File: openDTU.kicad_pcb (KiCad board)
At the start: 2 copper layers, 50 x 50 mm, 3 parts, among them U1 ESP32NodeMCU, U2 NRF24L01+PA+LNA_Breakout

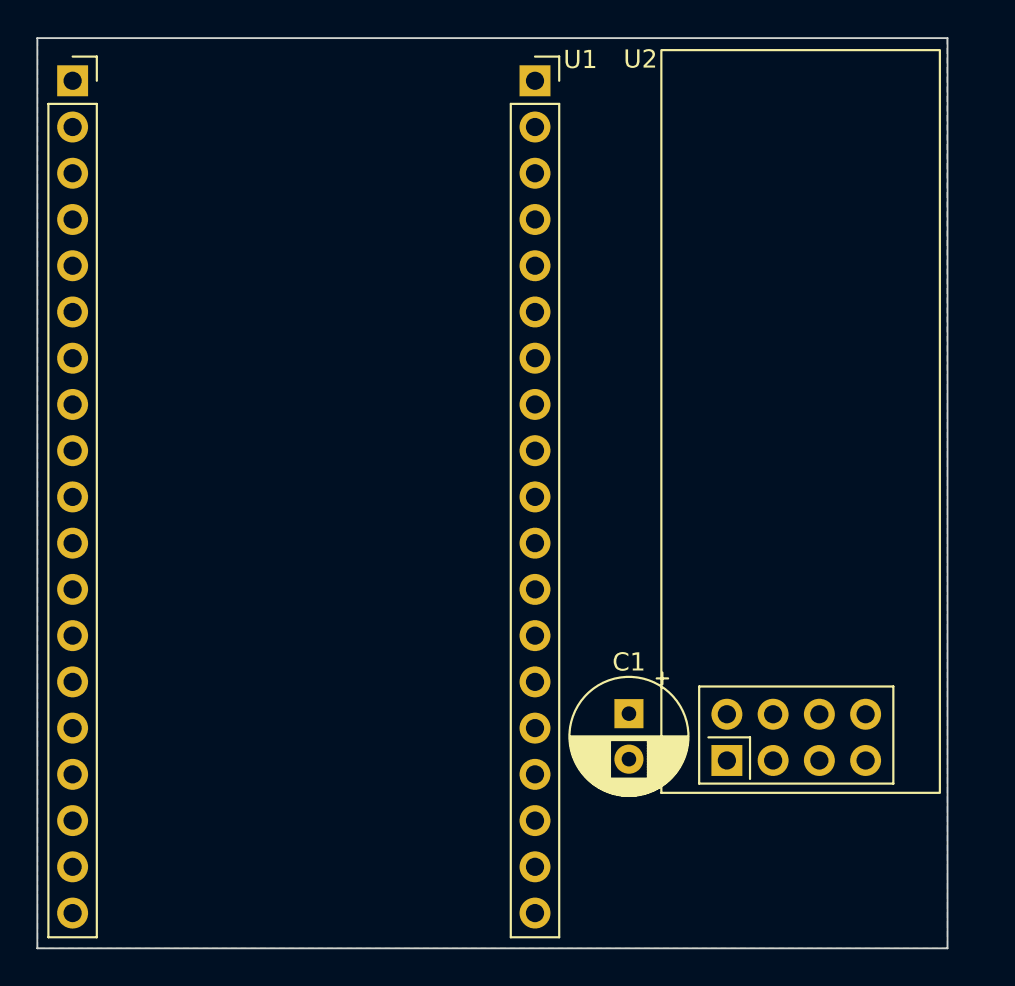
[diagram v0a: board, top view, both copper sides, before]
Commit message: connecting nRF24L01+ to the ESP32 in schematic
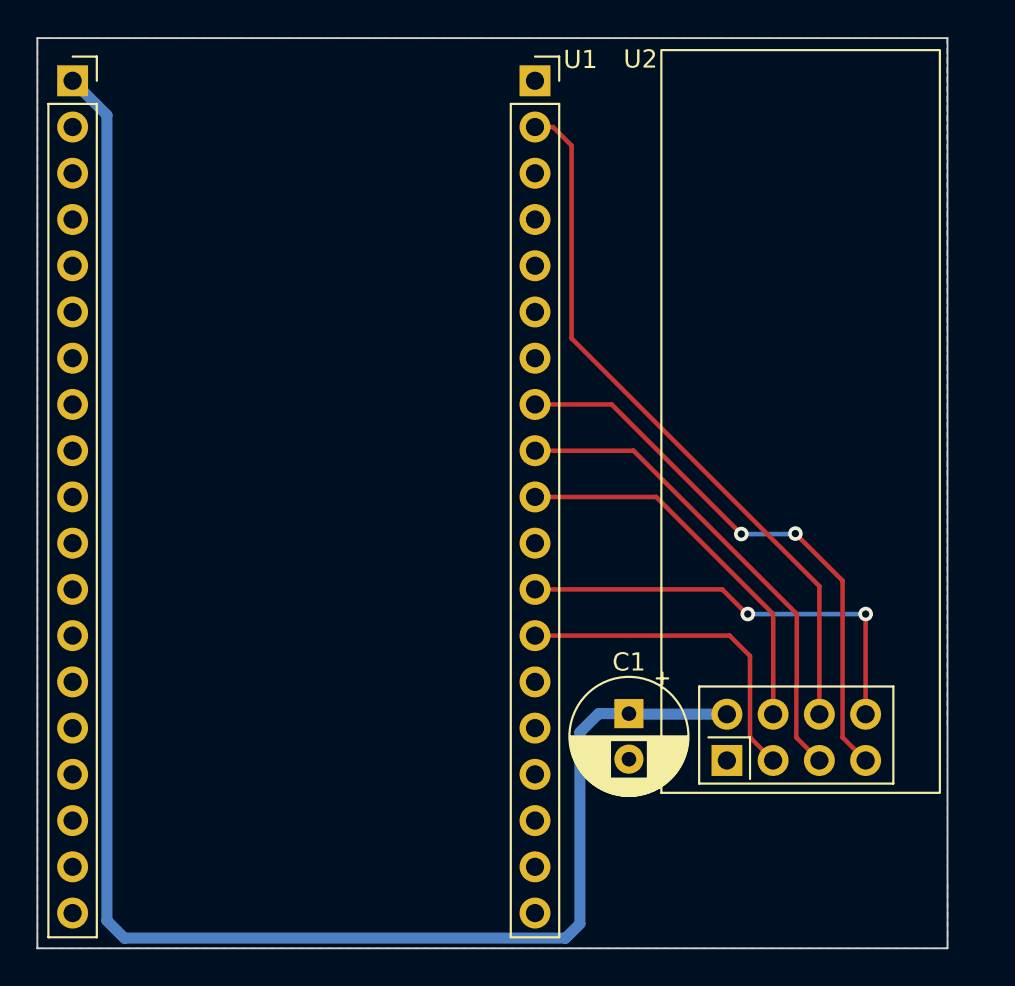
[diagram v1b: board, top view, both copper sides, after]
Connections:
- U1 pad 26: unconnected-(U1-Pad26) -> /CE
- U1 pad 27: unconnected-(U1-Pad27) -> /IRQ
- U1 pad 29: unconnected-(U1-Pad29) -> /~{CSN}
- U1 pad 30: unconnected-(U1-Pad30) -> /SCK
- U1 pad 31: unconnected-(U1-Pad31) -> /MISO
- U1 pad 37: unconnected-(U1-Pad37) -> /MOSI
- U2 pad 3: unconnected-(U2-Pad3) -> /CE
- U2 pad 4: unconnected-(U2-Pad4) -> /~{CSN}
- U2 pad 5: unconnected-(U2-Pad5) -> /SCK
- U2 pad 6: unconnected-(U2-Pad6) -> /MOSI
- U2 pad 7: unconnected-(U2-Pad7) -> /MISO
- U2 pad 8: unconnected-(U2-Pad8) -> /IRQ
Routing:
- net +3.3V: track 0.00 -> 92.7 mm
- net /MOSI: track 0.00 -> 39.3 mm
- net /MISO: track 0.00 -> 31.3 mm, vias 0 -> 2
- net /SCK: track 0.00 -> 26.7 mm
- net /IRQ: track 0.00 -> 24.2 mm, vias 0 -> 2
- net /~{CSN}: track 0.00 -> 21.3 mm
- net /CE: track 0.00 -> 18.5 mm
- added copper zone on F.Cu, net GND

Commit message: adding OpenDTU Logo and some informations on the silkscreen
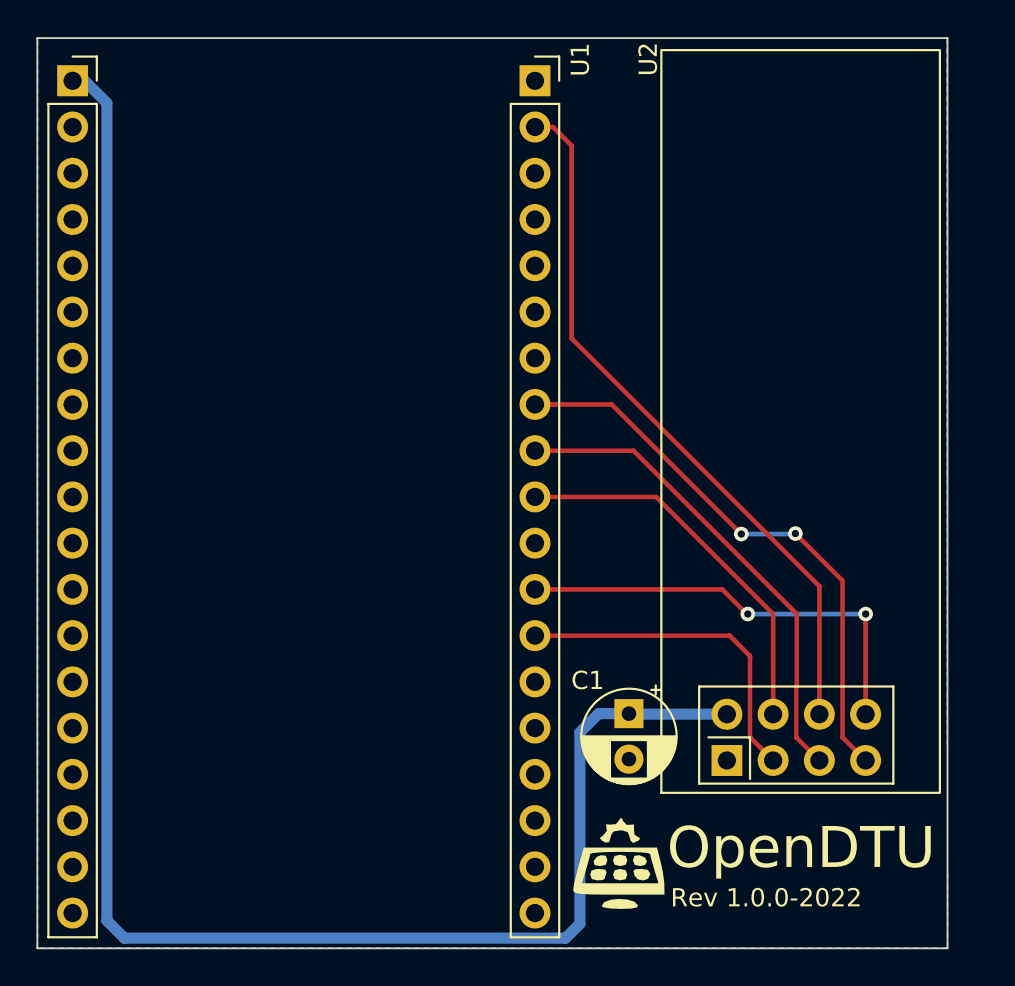
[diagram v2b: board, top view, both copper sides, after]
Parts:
- added G***: LOGO, OpenDTU_logo:OpenDTU, F.Cu at (152.1, 115.7)
- added REF**: KiCad-Logo2_5mm_SilkScreen, Symbol:KiCad-Logo2_5mm_SilkScreen, B.Cu at (159.3, 76.3)
- C1: footprint Capacitor_THT:CP_Radial_D6.3mm_P2.50mm -> Capacitor_THT:CP_Radial_D5.0mm_P2.50mm
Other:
- board text added: "OpenDTU"
- board text added: "Rev 1.0.0-2022"
- board text added: "https://github.com/dokuhn/openDTU-BreakoutBoard"

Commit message: chanching track width and adding mountinghole to support the NRF34L01+ Board
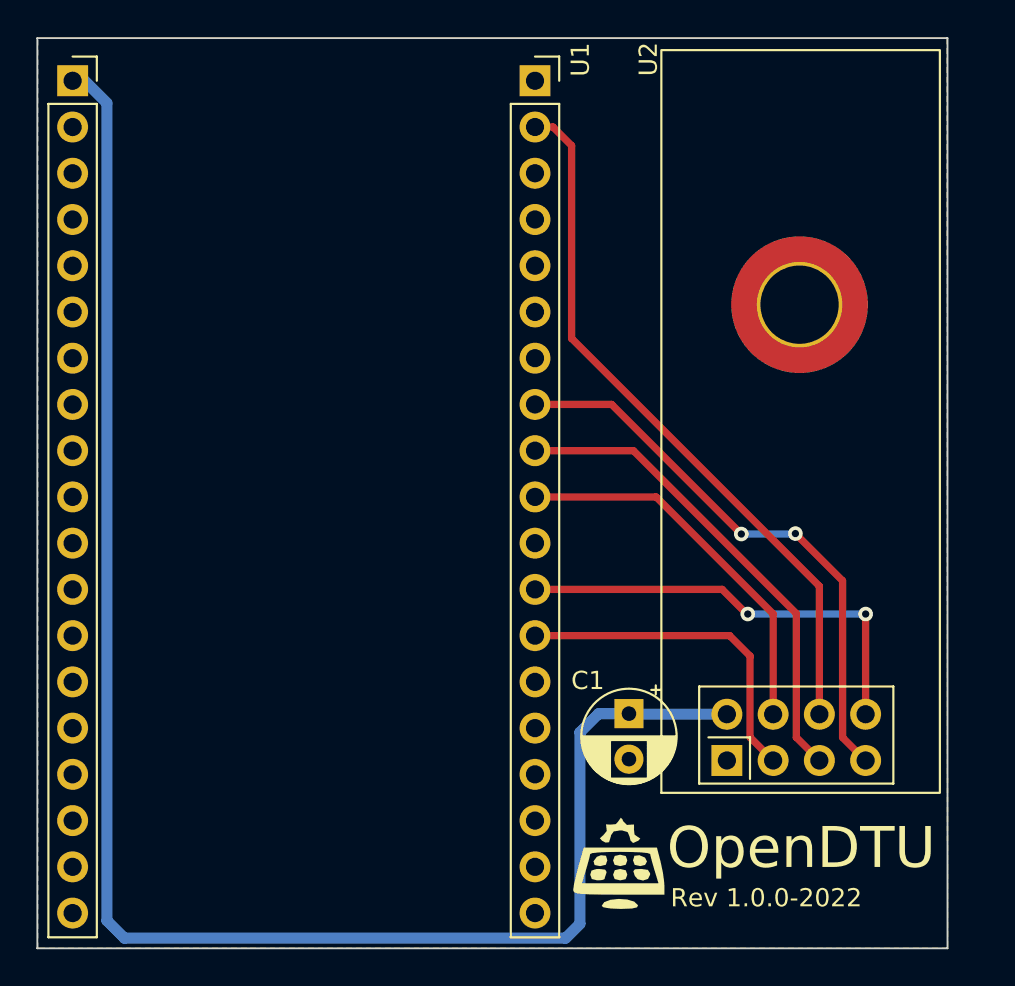
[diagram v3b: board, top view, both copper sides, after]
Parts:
- added REF**: MountingHole_4.3mm_M4_DIN965_Pad_TopBottom, MountingHole:MountingHole_4.3mm_M4_DIN965_Pad_TopBottom, F.Cu at (162.1, 85.0)
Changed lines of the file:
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@@
       ) (layer "F.SilkS") (width 0) (fill solid))
+  )
+  (footprint "MountingHole:MountingHole_4.3mm_M4_DIN965_Pad_TopBottom" (layer "F.Cu")
+    (at 162.052 85.0392)
+    (descr "Mounting Hole 4.3mm, M4, DIN965")
+    (tags "mounting hole 4.3mm m4 din965")
+    (attr board_only exclude_from_pos_files)
+    (fp_text reference "REF**" (at 0 -4.75) (layer "F.SilkS") hide
+      (effects (font (size 1 1) (thickness 0.15)))
+    )
+    (fp_text value "MountingHole_4.3mm_M4_DIN965_Pad_TopBottom" (at 0 4.75) (layer "F.Fab") hide
+      (effects (font (size 1 1) (thickness 0.15)))
+    )
+    (fp_text user "${REFERENCE}" (at 0 0) (layer "F.Fab") hide
+      (effects (font (size 1 1) (thickness 0.15)))
+    )
+    (fp_circle (center 0 0) (end 3.75 0) (layer "Cmts.User") (width 0.15) (fill none))
+    (fp_circle (center 0 0) (end 4 0) (layer "F.CrtYd") (width 0.05) (fill none))
+    (pad "1" thru_hole circle (at 0 0) (size 4.7 4.7) (drill 4.3) (layers *.Cu *.Mask)
+      (net 14 "GND"))
+    (pad "1" connect circle (at 0 0) (size 7.5 7.5) (layers "B.Cu" "B.Mask")
+      (net 14 "GND"))
+    (pad "1" connect circle (at 0 0) (size 7.5 7.5) (layers "F.Cu" "F.Mask")
+      (net 14 "GND"))
   )
   (footprint "Capacitor_THT:CP_Radial_D5.0mm_P2.50mm" (layer "F.Cu")
@@
   (segment (start 149.1996 119.8372) (end 149.987 119.0498) (width 0.6096) (layer "B.Cu") (net 1))
   (segment (start 151.016979 107.504221) (end 152.6794 107.504221) (width 0.6096) (layer "B.Cu") (net 1))
-  (segment (start 159.3342 108.8112) (end 159.3342 104.3432) (width 0.25) (layer "F.Cu") (net 26))
-  (segment (start 158.21 103.219) (end 147.519 103.219) (width 0.25) (layer "F.Cu") (net 26))
-  (segment (start 160.6 110.077) (end 159.3342 108.8112) (width 0.25) (layer "F.Cu") (net 26))
-  (segment (start 159.3342 104.3432) (end 158.21 103.219) (width 0.25) (layer "F.Cu") (net 26))
-  (segment (start 165.68 102.036) (end 165.68 107.537) (width 0.25) (layer "F.Cu") (net 27))
-  (segment (start 159.1564 102.0318) (end 157.8036 100.679) (width 0.25) (layer "F.Cu") (net 27))
+  (segment (start 159.3342 108.8112) (end 159.3342 104.3432) (width 0.4) (layer "F.Cu") (net 26))
+  (segment (start 158.21 103.219) (end 147.519 103.219) (width 0.4) (layer "F.Cu") (net 26))
+  (segment (start 160.6 110.077) (end 159.3342 108.8112) (width 0.4) (layer "F.Cu") (net 26))
+  (segment (start 159.3342 104.3432) (end 158.21 103.219) (width 0.4) (layer "F.Cu") (net 26))
+  (segment (start 165.68 102.036) (end 165.68 107.537) (width 0.4) (layer "F.Cu") (net 27))
+  (segment (start 159.1564 102.0318) (end 157.8036 100.679) (width 0.4) (layer "F.Cu") (net 27))
   (segment (start 159.2072 102.0318) (end 159.1564 102.0318) (width 0.25) (layer "F.Cu") (net 27))
-  (segment (start 157.8036 100.679) (end 147.519 100.679) (width 0.25) (layer "F.Cu") (net 27))
+  (segment (start 157.8036 100.679) (end 147.519 100.679) (width 0.4) (layer "F.Cu") (net 27))
   (segment (start 165.6842 102.0318) (end 165.68 102.036) (width 0.25) (layer "F.Cu") (net 27))
   (via (at 165.6842 102.0318) (size 0.8) (drill 0.4) (layers "F.Cu" "B.Cu") (net 27))
   (via (at 159.2072 102.0318) (size 0.8) (drill 0.4) (layers "F.Cu" "B.Cu") (net 27))
-  (segment (start 159.2072 102.0318) (end 165.6842 102.0318) (width 0.25) (layer "B.Cu") (net 27))
-  (segment (start 147.519 95.599) (end 154.1714 95.599) (width 0.25) (layer "F.Cu") (net 29))
-  (segment (start 160.6 102.0276) (end 160.6 107.537) (width 0.25) (layer "F.Cu") (net 29))
-  (segment (start 154.1714 95.599) (end 160.6 102.0276) (width 0.25) (layer "F.Cu") (net 29))
-  (segment (start 161.8996 105.9942) (end 161.8742 106.0196) (width 0.25) (layer "F.Cu") (net 30))
-  (segment (start 161.8996 102.0318) (end 161.8996 105.9942) (width 0.25) (layer "F.Cu") (net 30))
-  (segment (start 161.8742 106.0196) (end 161.8742 108.8112) (width 0.25) (layer "F.Cu") (net 30))
-  (segment (start 161.8742 108.8112) (end 163.14 110.077) (width 0.25) (layer "F.Cu") (net 30))
-  (segment (start 152.9268 93.059) (end 161.8996 102.0318) (width 0.25) (layer "F.Cu") (net 30))
-  (segment (start 147.519 93.059) (end 152.9268 93.059) (width 0.25) (layer "F.Cu") (net 30))
-  (segment (start 151.733 90.519) (end 147.519 90.519) (width 0.25) (layer "F.Cu") (net 31))
-  (segment (start 164.4142 100.203) (end 164.4142 108.8112) (width 0.25) (layer "F.Cu") (net 31))
-  (segment (start 164.4142 108.8112) (end 165.68 110.077) (width 0.25) (layer "F.Cu") (net 31))
-  (segment (start 161.8234 97.6122) (end 164.4142 100.203) (width 0.25) (layer "F.Cu") (net 31))
-  (segment (start 158.8516 97.6376) (end 151.733 90.519) (width 0.25) (layer "F.Cu") (net 31))
+  (segment (start 159.2072 102.0318) (end 165.6842 102.0318) (width 0.4) (layer "B.Cu") (net 27))
+  (segment (start 147.519 95.599) (end 154.1714 95.599) (width 0.4) (layer "F.Cu") (net 29))
+  (segment (start 160.6 102.0276) (end 160.6 107.537) (width 0.4) (layer "F.Cu") (net 29))
+  (segment (start 154.1714 95.599) (end 160.6 102.0276) (width 0.4) (layer "F.Cu") (net 29))
+  (segment (start 152.9268 93.059) (end 161.8742 102.0064) (width 0.4) (layer "F.Cu") (net 30))
+  (segment (start 161.8742 106.0196) (end 161.8742 108.8112) (width 0.4) (layer "F.Cu") (net 30))
+  (segment (start 161.8742 108.8112) (end 163.14 110.077) (width 0.4) (layer "F.Cu") (net 30))
+  (segment (start 161.8742 102.0064) (end 161.8742 105.9688) (width 0.4) (layer "F.Cu") (net 30))
+  (segment (start 147.519 93.059) (end 152.9268 93.059) (width 0.4) (layer "F.Cu") (net 30))
+  (segment (start 151.733 90.519) (end 147.519 90.519) (width 0.4) (layer "F.Cu") (net 31))
+  (segment (start 164.4142 100.203) (end 164.4142 108.8112) (width 0.4) (layer "F.Cu") (net 31))
+  (segment (start 164.4142 108.8112) (end 165.68 110.077) (width 0.4) (layer "F.Cu") (net 31))
+  (segment (start 161.8234 97.6122) (end 164.4142 100.203) (width 0.4) (layer "F.Cu") (net 31))
+  (segment (start 158.8516 97.6376) (end 151.733 90.519) (width 0.4) (layer "F.Cu") (net 31))
   (via (at 161.8234 97.6122) (size 0.8) (drill 0.4) (layers "F.Cu" "B.Cu") (net 31))
   (via (at 158.8516 97.6376) (size 0.8) (drill 0.4) (layers "F.Cu" "B.Cu") (net 31))
   (segment (start 161.798 97.6376) (end 161.8234 97.6122) (width 0.25) (layer "B.Cu") (net 31))
-  (segment (start 158.8516 97.6376) (end 161.798 97.6376) (width 0.25) (layer "B.Cu") (net 31))
-  (segment (start 163.14 100.5036) (end 163.14 107.537) (width 0.25) (layer "F.Cu") (net 36))
-  (segment (start 148.5072 75.279) (end 149.5298 76.3016) (width 0.25) (layer "F.Cu") (net 36))
-  (segment (start 149.5298 86.8934) (end 163.14 100.5036) (width 0.25) (layer "F.Cu") (net 36))
-  (segment (start 147.519 75.279) (end 148.5072 75.279) (width 0.25) (layer "F.Cu") (net 36))
-  (segment (start 149.5298 76.3016) (end 149.5298 86.8934) (width 0.25) (layer "F.Cu") (net 36))
+  (segment (start 158.8516 97.6376) (end 161.798 97.6376) (width 0.4) (layer "B.Cu") (net 31))
+  (segment (start 163.14 100.5036) (end 163.14 107.537) (width 0.4) (layer "F.Cu") (net 36))
+  (segment (start 148.5072 75.279) (end 149.5298 76.3016) (width 0.4) (layer "F.Cu") (net 36))
+  (segment (start 149.5298 86.8934) (end 163.14 100.5036) (width 0.4) (layer "F.Cu") (net 36))
+  (segment (start 147.519 75.279) (end 148.5072 75.279) (width 0.4) (layer "F.Cu") (net 36))
+  (segment (start 149.5298 76.3016) (end 149.5298 86.8934) (width 0.4) (layer "F.Cu") (net 36))
   (zone (net 14) (net_name "GND") (layers F&B.Cu) (hatch edge 0.508)
     (connect_pads (clearance 0.508))

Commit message: Adding some Testpads for signals between ESP32 and nRF24L01+. Adding vias to connect Bottom and Top GND Copper Zone.
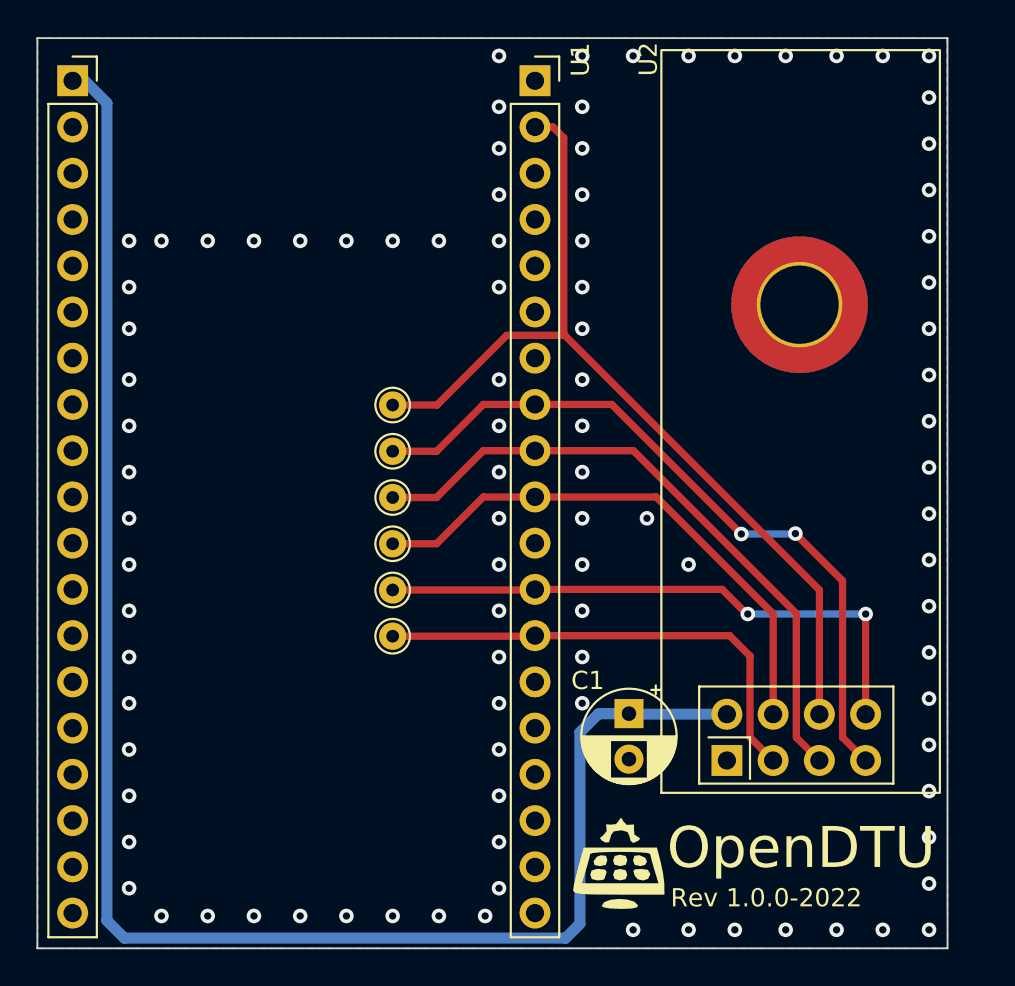
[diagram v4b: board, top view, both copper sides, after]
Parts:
- added TP1: TestPoint, TestPoint:TestPoint_THTPad_D1.5mm_Drill0.7mm, F.Cu at (139.7, 90.6)
- added TP2: TestPoint, TestPoint:TestPoint_THTPad_D1.5mm_Drill0.7mm, F.Cu at (139.7, 93.1)
- added TP3: TestPoint, TestPoint:TestPoint_THTPad_D1.5mm_Drill0.7mm, F.Cu at (139.7, 95.6)
- added TP4: TestPoint, TestPoint:TestPoint_THTPad_D1.5mm_Drill0.7mm, F.Cu at (139.7, 98.2)
- added TP5: TestPoint, TestPoint:TestPoint_THTPad_D1.5mm_Drill0.7mm, F.Cu at (139.7, 100.7)
- added TP6: TestPoint, TestPoint:TestPoint_THTPad_D1.5mm_Drill0.7mm, F.Cu at (139.7, 103.3)
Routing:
- net /MOSI: track 39.3 -> 50.4 mm
- net /SCK: track 26.6 -> 35.5 mm
- net /~{CSN}: track 21.3 -> 30.1 mm
- net /MISO: track 31.3 -> 40.2 mm
- net /CE: track 18.5 -> 26.4 mm
- net /IRQ: track 24.2 -> 32.1 mm
- net GND: vias 0 -> 97
